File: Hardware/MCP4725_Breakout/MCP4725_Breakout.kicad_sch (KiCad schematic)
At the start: 17 parts, among them J1 Conn_01x02, J2 I2C, U2 MCP4725

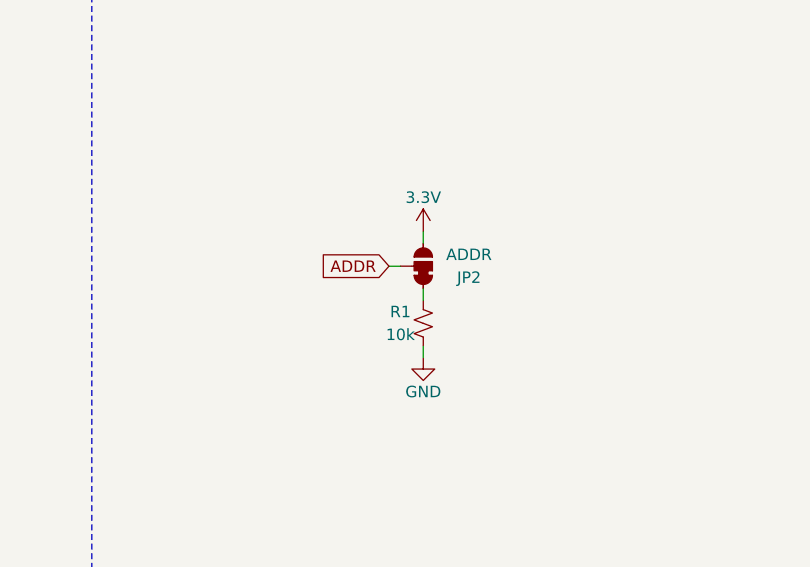
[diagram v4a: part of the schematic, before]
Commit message: Changes dual to single jumper
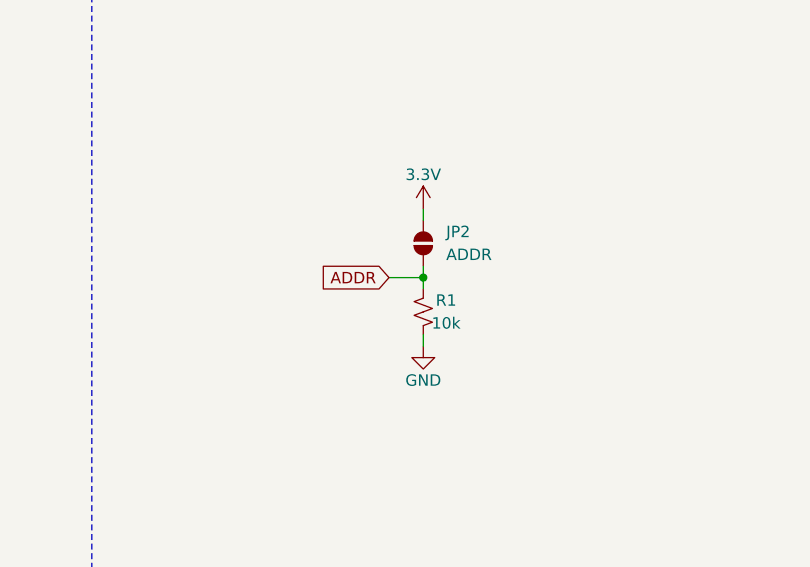
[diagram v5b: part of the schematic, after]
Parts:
- removed JP2: ADDR, SparkFun-Jumper:Jumper_3_NC-1_Trace, symbol SparkFun-Jumper:SolderJumper_3_Bridged12
- added JP2: ADDR, SparkFun-Jumper:Jumper_2_NO, symbol SparkFun-Jumper:SolderJumper_2_Open
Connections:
- net 3.3V: now also JP2.2 (B)
- net ADDR: now also R1.2, JP2.1 (A)
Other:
- moved on the sheet: R1
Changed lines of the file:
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@@
+	)
+	(junction
+		(at 139.7 133.35)
+		(diameter 0)
+		(color 0 0 0 0)
 	)
 	(junction
@@
 	(wire
 		(pts
-			(xy 135.89 132.08) (xy 137.16 132.08)
+			(xy 135.89 133.35) (xy 139.7 133.35)
 		)
 		(stroke
@@
 	(wire
 		(pts
+			(xy 139.7 133.35) (xy 139.7 134.62)
+		)
+		(stroke
+			(width 0)
+			(type default)
+		)
+	)
+	(wire
+		(pts
 			(xy 58.42 149.86) (xy 59.69 149.86)
 		)
@@
 	(wire
 		(pts
-			(xy 139.7 142.24) (xy 139.7 140.97)
+			(xy 139.7 140.97) (xy 139.7 139.7)
 		)
 		(stroke
@@
 	(wire
 		(pts
-			(xy 139.7 134.62) (xy 139.7 135.89)
+			(xy 139.7 132.08) (xy 139.7 133.35)
 		)
 		(stroke
@@
 	(wire
 		(pts
-			(xy 139.7 128.27) (xy 139.7 129.54)
+			(xy 139.7 125.73) (xy 139.7 127)
 		)
 		(stroke
@@
 	(global_label "ADDR"
 		(shape input)
-		(at 135.89 132.08 180)
+		(at 135.89 133.35 180)
 		(fields_autoplaced yes)
 		(effects
@@
 		)
 		(property "Intersheetrefs" "${INTERSHEET_REFS}"
-			(at 128.0062 132.08 0)
+			(at 128.0062 133.35 0)
 			(effects
 				(font
@@
 				(justify left)
 				(hide yes)
-			)
-		)
-	)
-	(symbol
-		(lib_id "SparkFun-Jumper:SolderJumper_3_Bridged12")
-		(at 139.7 132.08 270)
-		(mirror x)
-		(unit 1)
-		(exclude_from_sim no)
-		(in_bom yes)
-		(on_board yes)
-		(dnp no)
-		(property "Reference" "JP2"
-			(at 144.78 133.35 90)
-			(effects
-				(font
-					(size 1.27 1.27)
-				)
-			)
-		)
-		(property "Value" "ADDR"
-			(at 144.78 130.81 90)
-			(effects
-				(font
-					(size 1.27 1.27)
-				)
-			)
-		)
-		(property "Footprint" "SparkFun-Jumper:Jumper_3_NC-1_Trace"
-			(at 134.62 132.08 0)
-			(effects
-				(font
-					(size 1.27 1.27)
-				)
-				(hide yes)
-			)
-		)
-		(property "Datasheet" "~"
-			(at 132.08 132.08 0)
-			(effects
-				(font
-					(size 1.27 1.27)
-				)
-				(hide yes)
-			)
-		)
-		(property "Description" "3-pole Solder Jumper, pins 1+2 closed/bridged"
-			(at 129.54 132.08 0)
-			(effects
-				(font
-					(size 1.27 1.27)
-				)
-				(hide yes)
-			)
-		)
-		(pin "2"
-		)
-		(pin "1"
-		)
-		(pin "3"
-		)
-		(instances
-			(project ""
-				(path "/bf35e96c-ec8b-4540-83a4-3cc6df170383"
-					(reference "JP2")
-					(unit 1)
-				)
 			)
 		)
@@
 	(symbol
 		(lib_id "SparkFun-Resistor:10k_0603")
-		(at 139.7 138.43 90)
+		(at 139.7 137.16 270)
+		(mirror x)
 		(unit 1)
 		(exclude_from_sim no)
@@
 		(dnp no)
 		(property "Reference" "R1"
-			(at 137.16 137.16 90)
+			(at 142.24 135.89 90)
 			(effects
 				(font
@@
 		)
 		(property "Value" "10k"
-			(at 137.16 139.7 90)
+			(at 142.24 138.43 90)
 			(effects
 				(font
@@
 		)
 		(property "Footprint" "SparkFun-Resistor:R_0603_1608Metric"
-			(at 144.018 138.43 0)
+			(at 135.382 137.16 0)
 			(effects
 				(font
@@
 		)
 		(property "Datasheet" "https://www.vishay.com/docs/20035/dcrcwe3.pdf"
-			(at 148.59 138.43 0)
+			(at 130.81 137.16 0)
 			(effects
 				(font
@@
 		)
 		(property "Description" "Resistor"
-			(at 151.13 138.43 0)
+			(at 128.27 137.16 0)
 			(effects
 				(font
@@
 		)
 		(property "PROD_ID" "RES-00824"
-			(at 146.05 138.43 0)
+			(at 133.35 137.16 0)
 			(effects
 				(font
@@
 	)
 	(symbol
+		(lib_id "SparkFun-Jumper:SolderJumper_2_Open")
+		(at 139.7 129.54 90)
+		(unit 1)
+		(exclude_from_sim no)
+		(in_bom yes)
+		(on_board yes)
+		(dnp no)
+		(fields_autoplaced yes)
+		(property "Reference" "JP2"
+			(at 142.24 128.2699 90)
+			(effects
+				(font
+					(size 1.27 1.27)
+				)
+				(justify right)
+			)
+		)
+		(property "Value" "ADDR"
+			(at 142.24 130.8099 90)
+			(effects
+				(font
+					(size 1.27 1.27)
+				)
+				(justify right)
+			)
+		)
+		(property "Footprint" "SparkFun-Jumper:Jumper_2_NO"
+			(at 143.002 129.54 0)
+			(effects
+				(font
+					(size 1.27 1.27)
+				)
+				(hide yes)
+			)
+		)
+		(property "Datasheet" "~"
+			(at 146.05 129.54 0)
+			(effects
+				(font
+					(size 1.27 1.27)
+				)
+				(hide yes)
+			)
+		)
+		(property "Description" "Solder Jumper, 2-pole, open"
+			(at 148.59 129.54 0)
+			(effects
+				(font
+					(size 1.27 1.27)
+				)
+				(hide yes)
+			)
+		)
+		(pin "2"
+		)
+		(pin "1"
+		)
+		(instances
+			(project ""
+				(path "/bf35e96c-ec8b-4540-83a4-3cc6df170383"
+					(reference "JP2")
+					(unit 1)
+				)
+			)
+		)
+	)
+	(symbol
 		(lib_id "SparkFun-PowerSymbol:3.3V")
 		(at 54.61 135.89 0)
@@
 	(symbol
 		(lib_id "SparkFun-PowerSymbol:GND")
-		(at 139.7 142.24 0)
+		(at 139.7 140.97 0)
 		(unit 1)
 		(exclude_from_sim no)
@@
 		(fields_autoplaced yes)
 		(property "Reference" "#PWR02"
-			(at 139.7 148.59 0)
+			(at 139.7 147.32 0)
 			(effects
 				(font
@@
 		)
 		(property "Value" "GND"
-			(at 139.7 146.05 0)
+			(at 139.7 144.78 0)
 			(do_not_autoplace yes)
 			(effects
@@
 		)
 		(property "Footprint" ""
-			(at 139.7 142.24 0)
+			(at 139.7 140.97 0)
 			(effects
 				(font
@@
 		)
 		(property "Datasheet" ""
-			(at 139.7 142.24 0)
+			(at 139.7 140.97 0)
 			(effects
 				(font
@@
 		)
 		(property "Description" "Power symbol creates a global label with name \"GND\" , ground"
-			(at 139.7 151.13 0)
+			(at 139.7 149.86 0)
 			(effects
 				(font
@@
 	(symbol
 		(lib_id "SparkFun-PowerSymbol:3.3V")
-		(at 139.7 128.27 0)
+		(at 139.7 125.73 0)
 		(unit 1)
 		(exclude_from_sim no)
@@
 		(on_board yes)
 		(dnp no)
-		(fields_autoplaced yes)
 		(property "Reference" "#PWR03"
+			(at 139.7 129.54 0)
+			(effects
+				(font
+					(size 1.27 1.27)
+				)
+				(hide yes)
+			)
+		)
+		(property "Value" "3.3V"
+			(at 139.7 121.92 0)
+			(do_not_autoplace yes)
+			(effects
+				(font
+					(size 1.27 1.27)
+				)
+			)
+		)
+		(property "Footprint" ""
+			(at 139.7 125.73 0)
+			(effects
+				(font
+					(size 1.27 1.27)
+				)
+				(hide yes)
+			)
+		)
+		(property "Datasheet" ""
+			(at 139.7 125.73 0)
+			(effects
+				(font
+					(size 1.27 1.27)
+				)
+				(hide yes)
+			)
+		)
+		(property "Description" "Power symbol creates a global label with name \"3.3V\""
 			(at 139.7 132.08 0)
 			(effects
 				(font
-					(size 1.27 1.27)
-				)
-				(hide yes)
-			)
-		)
-		(property "Value" "3.3V"
-			(at 139.7 124.46 0)
-			(do_not_autoplace yes)
-			(effects
-				(font
-					(size 1.27 1.27)
-				)
-			)
-		)
-		(property "Footprint" ""
-			(at 139.7 128.27 0)
-			(effects
-				(font
-					(size 1.27 1.27)
-				)
-				(hide yes)
-			)
-		)
-		(property "Datasheet" ""
-			(at 139.7 128.27 0)
-			(effects
-				(font
-					(size 1.27 1.27)
-				)
-				(hide yes)
-			)
-		)
-		(property "Description" "Power symbol creates a global label with name \"3.3V\""
-			(at 139.7 134.62 0)
-			(effects
-				(font

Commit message: Fixes jumpers on more time
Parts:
- removed JP2: ADDR, SparkFun-Jumper:Jumper_2_NO, symbol SparkFun-Jumper:SolderJumper_2_Open
- added JP2: ADDR, SparkFun-Jumper:Jumper_2_NC_Trace, symbol SparkFun-Jumper:SolderJumper_2_Bridged
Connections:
- net 3.3V: now also R1.2
- net ADDR: now also R1.1, JP2.2 (B); no longer R1.2
- net GND: now also JP2.1 (A); no longer R1.1
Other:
- moved on the sheet: R1
